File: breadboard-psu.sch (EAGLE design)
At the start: 22 parts, among them J1 163-5010-E, J3 5V-CABLE, J5 3.3V-CABLE, K1 GF-126-0159, K2 GF-126-0159, K3 GF-126-0159, U1 AP1117T50G-U, U2 AP1117T33G-U

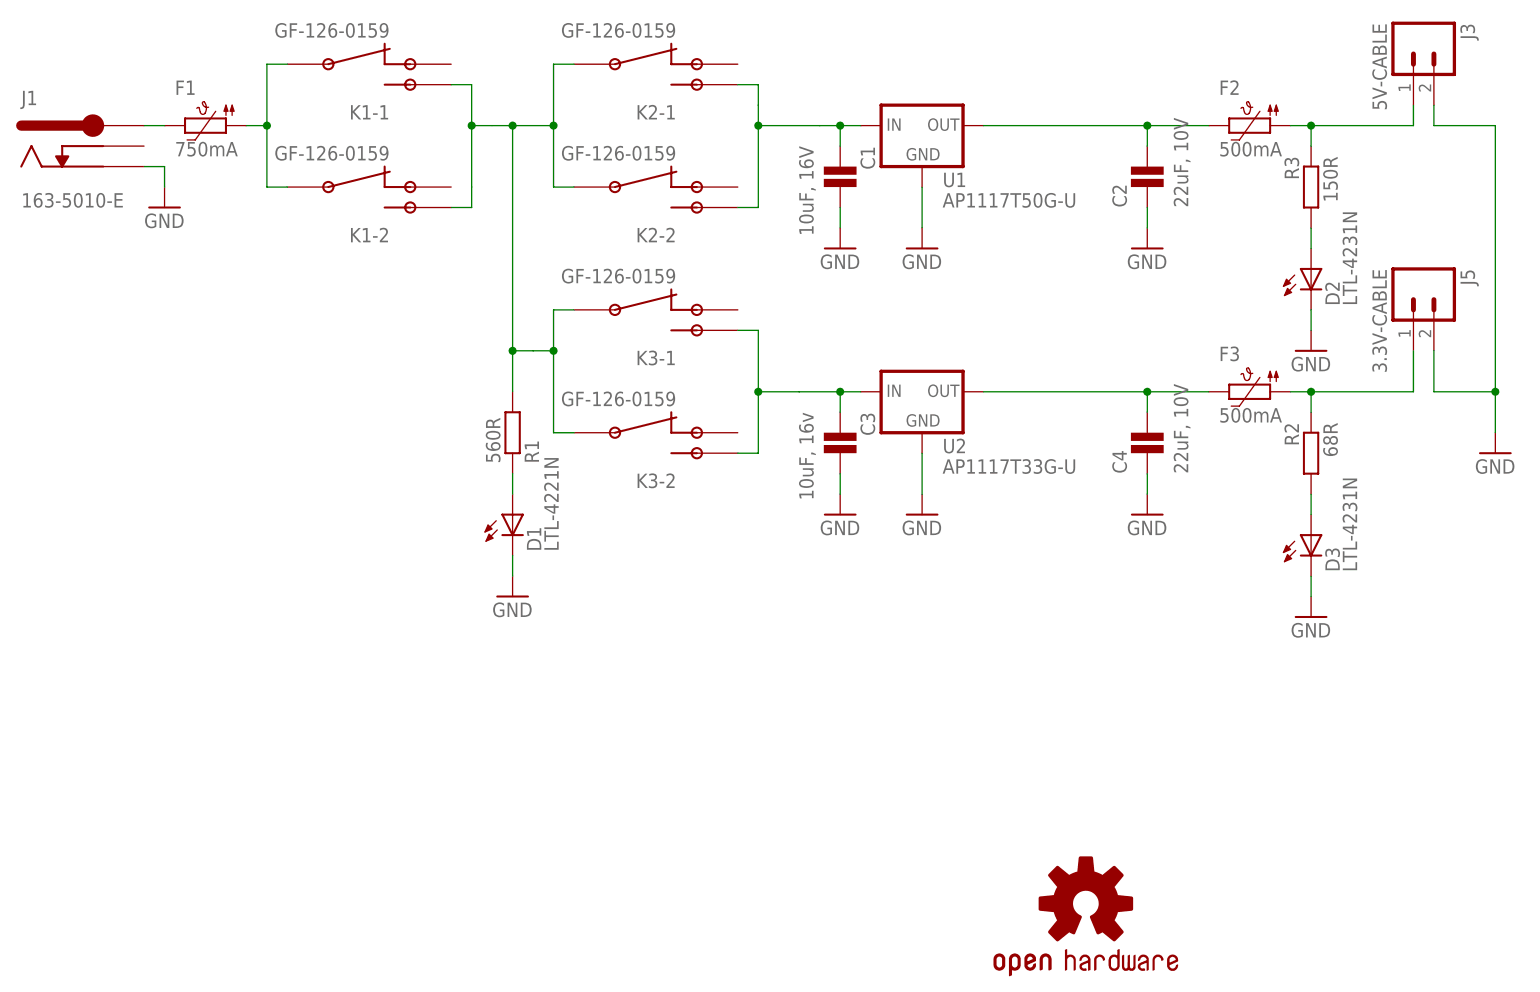
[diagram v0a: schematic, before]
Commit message: Adjustments after the trial fab run:  - enlarged in X dimension, still fits in 5x5cm  - moved power LED behind DC jack, better contrast and visibility  - enlarged legend text for switches and added signage for the ON position.
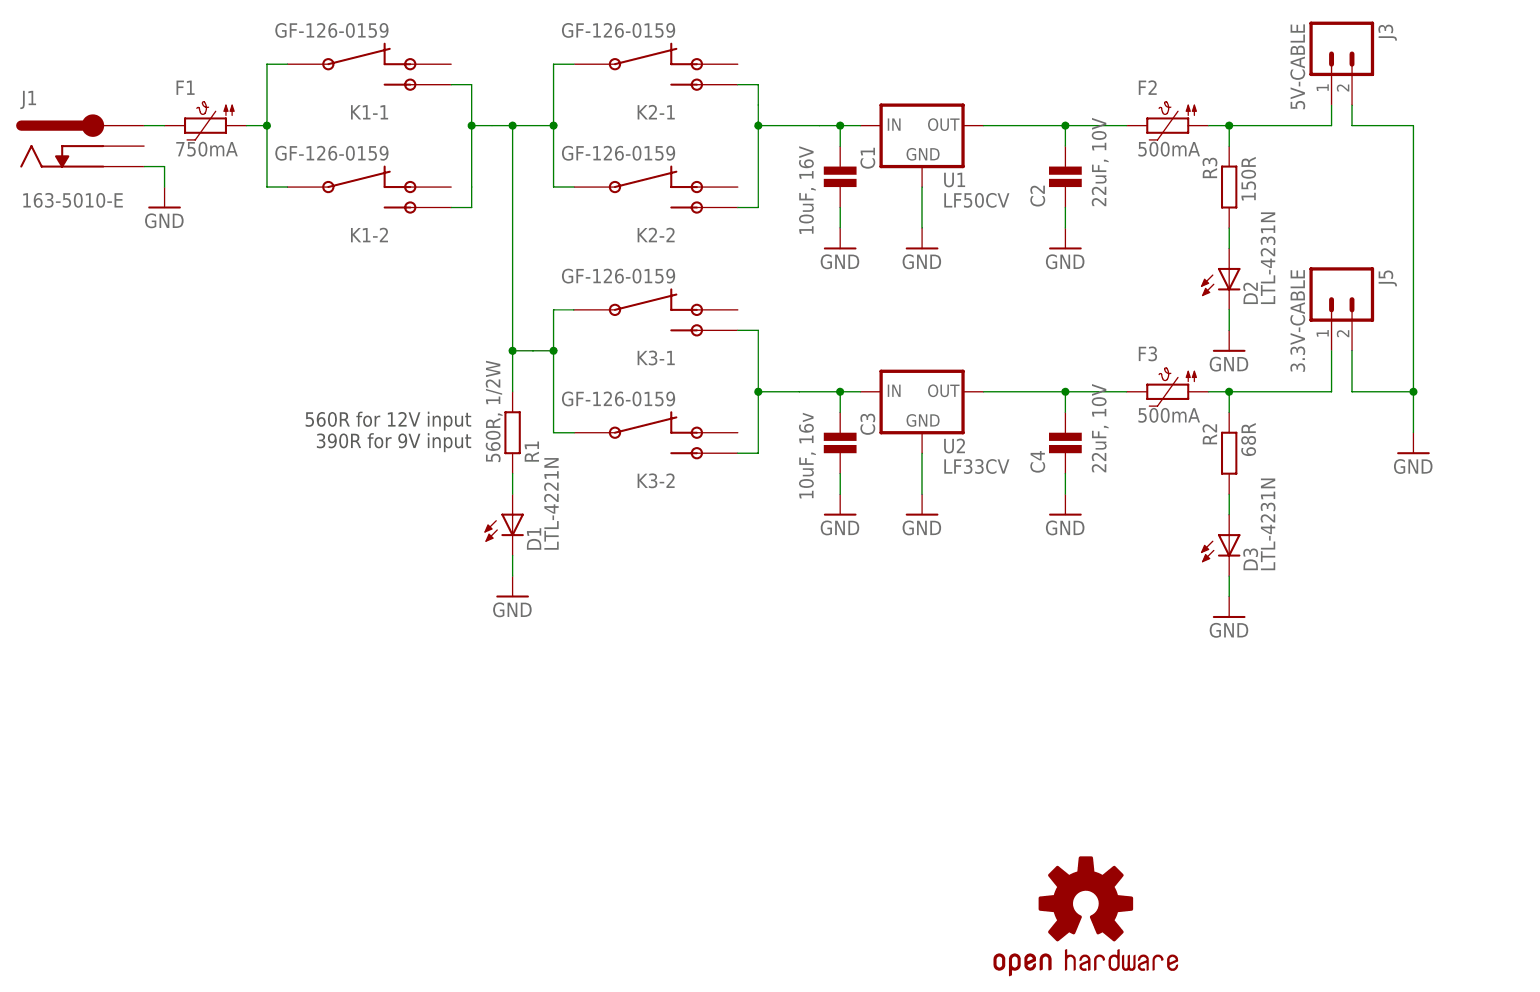
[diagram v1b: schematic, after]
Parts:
- R1: value 560R -> 560R, 1/2W
- U1: value AP1117T50G-U -> LF50CV
- U2: value AP1117T33G-U -> LF33CV
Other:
- note added: "560R for 12V input 390R for 9V input"
- note added: "On heatsink"
- moved on the sheet: C2, C4, D2, D3, F2, F3, J3, J5, R2, R3
